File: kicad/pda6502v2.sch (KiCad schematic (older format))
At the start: 87 parts, among them J1 GPIO1, J2 GPIO2, J3 UART, J4 Screw_Terminal_01x02, J5 Conn_02x04_Odd_Even, J6 ICSP, J7 SPI, J8 FPGA_EXT, J9 SID, SW1 SW_Push, SW2 SW_Push, U1 W65C02SxP, U10 LT3030, U11 SC28L92A1B, U2 W65C22SxP, U3 W65C22SxP, U4 DS1818, U5 AS6C4008-55PCN, U6 ARMSID, U7 AT25M01, U8 ICE40HX4K-TQ144, U9 TLV1117-33, X1 8 MHz, X2 3.6864 MHz

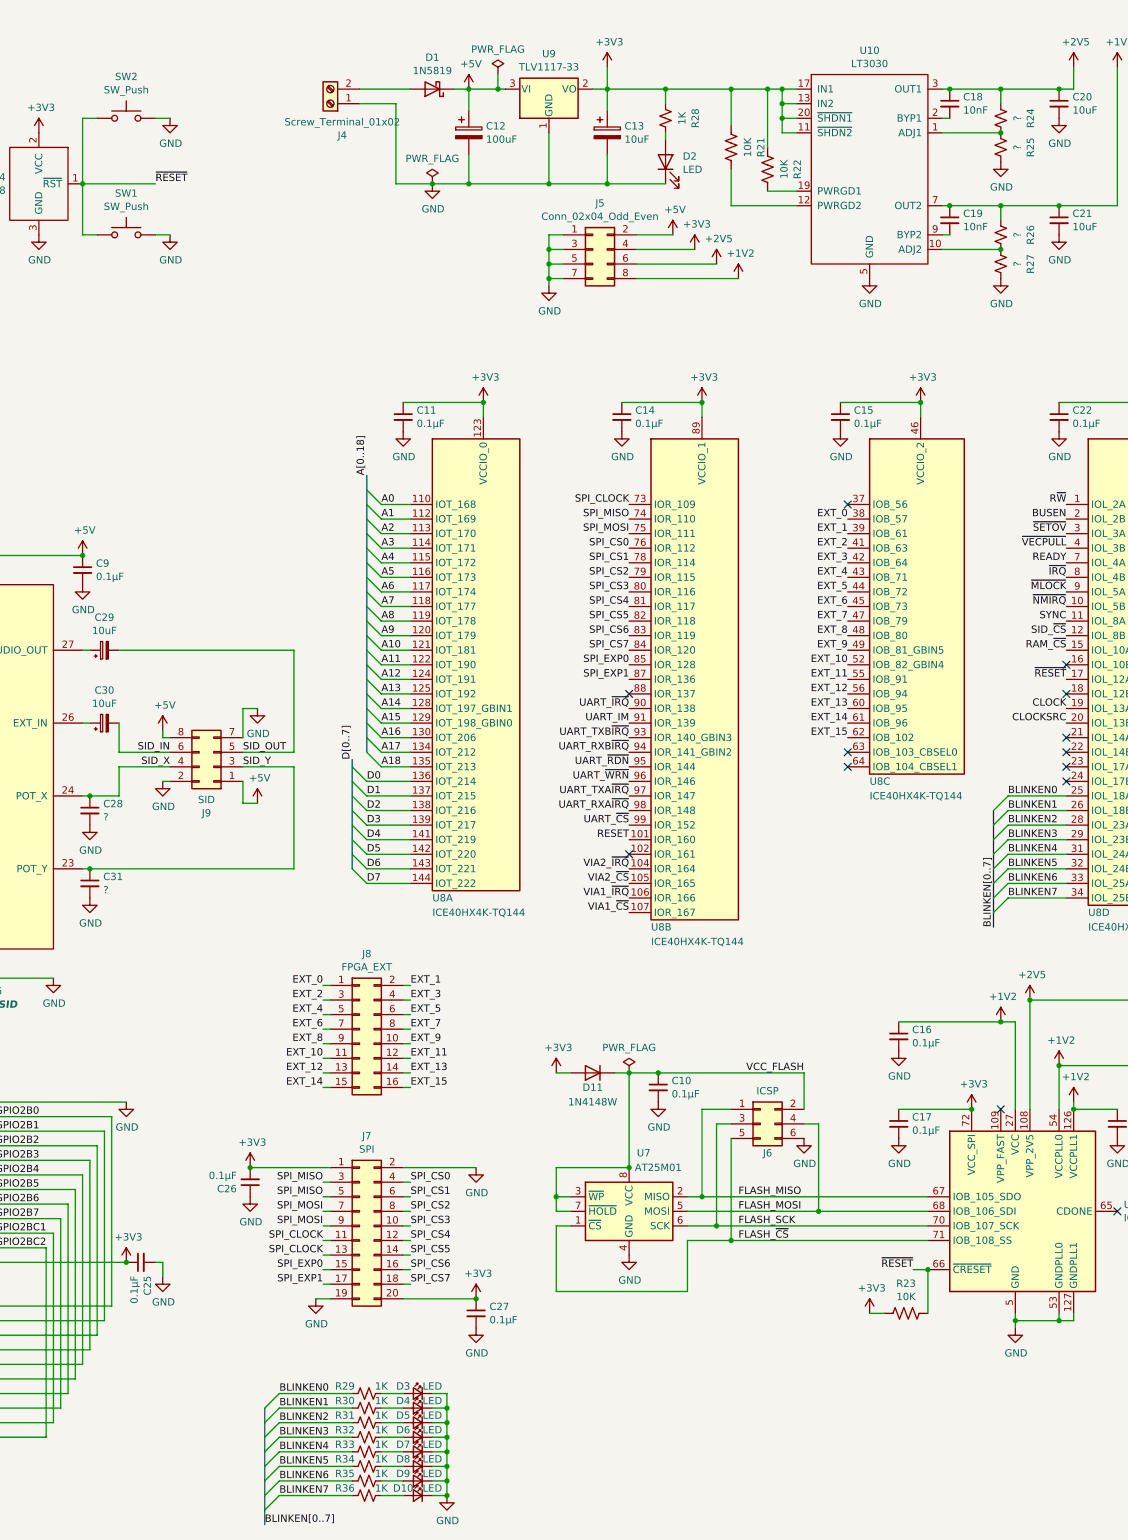
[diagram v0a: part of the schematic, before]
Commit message: kicad: post-fab changes (mostly/entirely R/C value updates?)
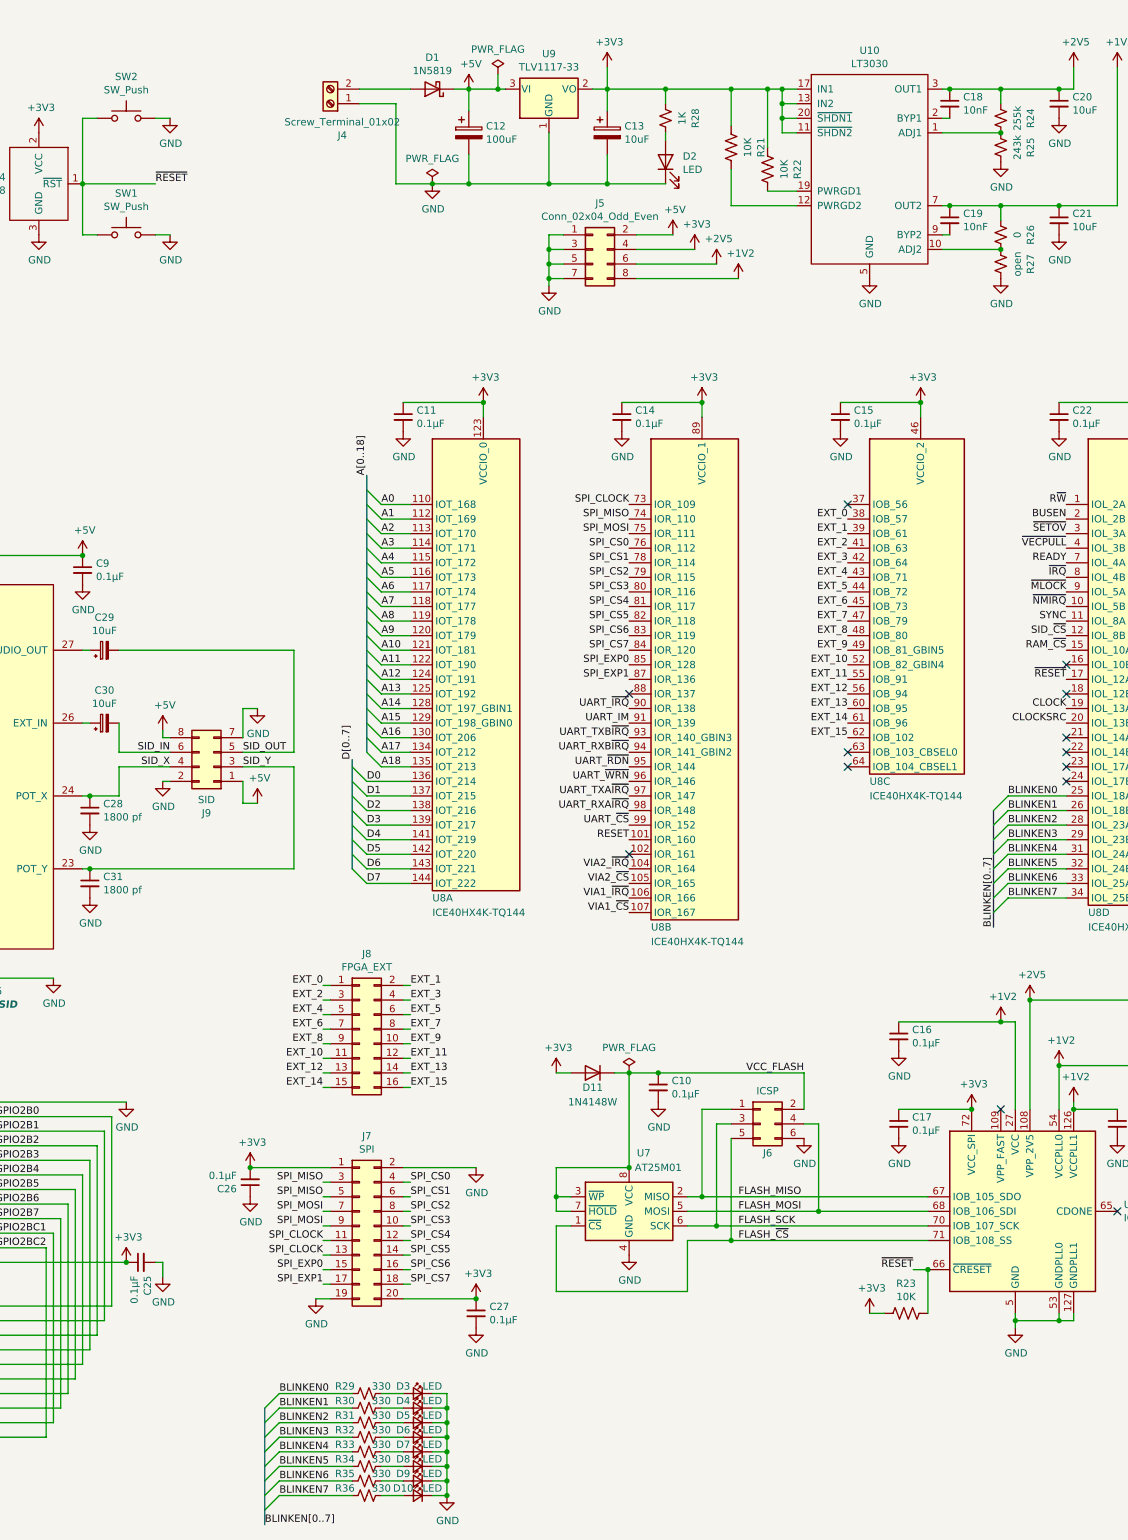
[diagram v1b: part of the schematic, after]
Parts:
- C28, C31: value ? -> 1800 pf
- R24: value ? -> 255k
- R25: value ? -> 243k
- R26: value ? -> 0
- R27: value ? -> open
- R29, R30, R31, R32, R33, R34, R35, R36: value 1K -> 330
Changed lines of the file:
@@
 AR Path="/627F29DB" Ref="R24"  Part="1"
 F 0 "R24" V 14095 1300 50  0000 C CNN
-F 1 "?" V 14186 1300 50  0000 C CNN
+F 1 "255k" V 14186 1300 50  0000 C CNN
 F 2 "Resistor_SMD:R_0805_2012Metric_Pad1.20x1.40mm_HandSolder" V 14340 1290 50  0001 C CNN
 F 3 "~" H 14300 1300 50  0001 C CNN
@@
 AR Path="/629F2F05" Ref="R26"  Part="1"
 F 0 "R26" V 14095 2100 50  0000 C CNN
-F 1 "?" V 14186 2100 50  0000 C CNN
+F 1 "0" V 14186 2100 50  0000 C CNN
 F 2 "Resistor_SMD:R_0805_2012Metric_Pad1.20x1.40mm_HandSolder" V 14340 2090 50  0001 C CNN
 F 3 "~" H 14300 2100 50  0001 C CNN
@@
 AR Path="/62A257C4" Ref="R27"  Part="1"
 F 0 "R27" V 14095 2300 50  0000 C CNN
-F 1 "?" V 14186 2300 50  0000 C CNN
+F 1 "open" V 14186 2300 50  0000 C CNN
 F 2 "Resistor_SMD:R_0805_2012Metric_Pad1.20x1.40mm_HandSolder" V 14340 2290 50  0001 C CNN
 F 3 "~" H 14300 2300 50  0001 C CNN
@@
 AR Path="/629F2897" Ref="R25"  Part="1"
 F 0 "R25" V 14095 1500 50  0000 C CNN
-F 1 "?" V 14186 1500 50  0000 C CNN
+F 1 "243k" V 14186 1500 50  0000 C CNN
 F 2 "Resistor_SMD:R_0805_2012Metric_Pad1.20x1.40mm_HandSolder" V 14340 1490 50  0001 C CNN
 F 3 "~" H 14300 1500 50  0001 C CNN
@@
 P 9950 10050
 F 0 "R29" V 9900 9900 50  0000 C CNN
-F 1 "1K" V 9900 10150 50  0000 C CNN
+F 1 "330" V 9900 10150 50  0000 C CNN
 F 2 "Resistor_SMD:R_0805_2012Metric_Pad1.20x1.40mm_HandSolder" H 9950 10050 50  0001 C CNN
 F 3 "~" H 9950 10050 50  0001 C CNN
@@
 P 9950 10150
 F 0 "R30" V 9900 10000 50  0000 C CNN
-F 1 "1K" V 9900 10250 50  0000 C CNN
+F 1 "330" V 9900 10250 50  0000 C CNN
 F 2 "Resistor_SMD:R_0805_2012Metric_Pad1.20x1.40mm_HandSolder" H 9950 10150 50  0001 C CNN
 F 3 "~" H 9950 10150 50  0001 C CNN
@@
 P 9950 10250
 F 0 "R31" V 9900 10100 50  0000 C CNN
-F 1 "1K" V 9900 10350 50  0000 C CNN
+F 1 "330" V 9900 10350 50  0000 C CNN
 F 2 "Resistor_SMD:R_0805_2012Metric_Pad1.20x1.40mm_HandSolder" H 9950 10250 50  0001 C CNN
 F 3 "~" H 9950 10250 50  0001 C CNN
@@
 P 9950 10350
 F 0 "R32" V 9900 10200 50  0000 C CNN
-F 1 "1K" V 9900 10450 50  0000 C CNN
+F 1 "330" V 9900 10450 50  0000 C CNN
 F 2 "Resistor_SMD:R_0805_2012Metric_Pad1.20x1.40mm_HandSolder" H 9950 10350 50  0001 C CNN
 F 3 "~" H 9950 10350 50  0001 C CNN
@@
 P 9950 10450
 F 0 "R33" V 9900 10300 50  0000 C CNN
-F 1 "1K" V 9900 10550 50  0000 C CNN
+F 1 "330" V 9900 10550 50  0000 C CNN
 F 2 "Resistor_SMD:R_0805_2012Metric_Pad1.20x1.40mm_HandSolder" H 9950 10450 50  0001 C CNN
 F 3 "~" H 9950 10450 50  0001 C CNN
@@
 P 9950 10550
 F 0 "R34" V 9900 10400 50  0000 C CNN
-F 1 "1K" V 9900 10650 50  0000 C CNN
+F 1 "330" V 9900 10650 50  0000 C CNN
 F 2 "Resistor_SMD:R_0805_2012Metric_Pad1.20x1.40mm_HandSolder" H 9950 10550 50  0001 C CNN
 F 3 "~" H 9950 10550 50  0001 C CNN
@@
 P 9950 10650
 F 0 "R35" V 9900 10500 50  0000 C CNN
-F 1 "1K" V 9900 10750 50  0000 C CNN
+F 1 "330" V 9900 10750 50  0000 C CNN
 F 2 "Resistor_SMD:R_0805_2012Metric_Pad1.20x1.40mm_HandSolder" H 9950 10650 50  0001 C CNN
 F 3 "~" H 9950 10650 50  0001 C CNN
@@
 P 9950 10750
 F 0 "R36" V 9900 10600 50  0000 C CNN
-F 1 "1K" V 9900 10850 50  0000 C CNN
+F 1 "330" V 9900 10850 50  0000 C CNN
 F 2 "Resistor_SMD:R_0805_2012Metric_Pad1.20x1.40mm_HandSolder" H 9950 10750 50  0001 C CNN
 F 3 "~" H 9950 10750 50  0001 C CNN
@@
 P 8050 6050
 F 0 "C28" H 8142 6096 50  0000 L CNN
-F 1 "?" H 8142 6005 50  0000 L CNN
+F 1 "1800 pf" H 8142 6005 50  0000 L CNN
 F 2 "Capacitor_SMD:C_0805_2012Metric_Pad1.18x1.45mm_HandSolder" H 8050 6050 50  0001 C CNN
 F 3 "~" H 8050 6050 50  0001 C CNN
@@
 P 8050 6550
 F 0 "C31" H 8142 6596 50  0000 L CNN
-F 1 "?" H 8142 6505 50  0000 L CNN
+F 1 "1800 pf" H 8142 6505 50  0000 L CNN
 F 2 "Capacitor_SMD:C_0805_2012Metric_Pad1.18x1.45mm_HandSolder" H 8050 6550 50  0001 C CNN
 F 3 "~" H 8050 6550 50  0001 C CNN
